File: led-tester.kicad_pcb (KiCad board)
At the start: 2 copper layers, 79.7 x 19.1 mm, 23 parts, among them M1 Arduino_Mini, U1 PCF8591

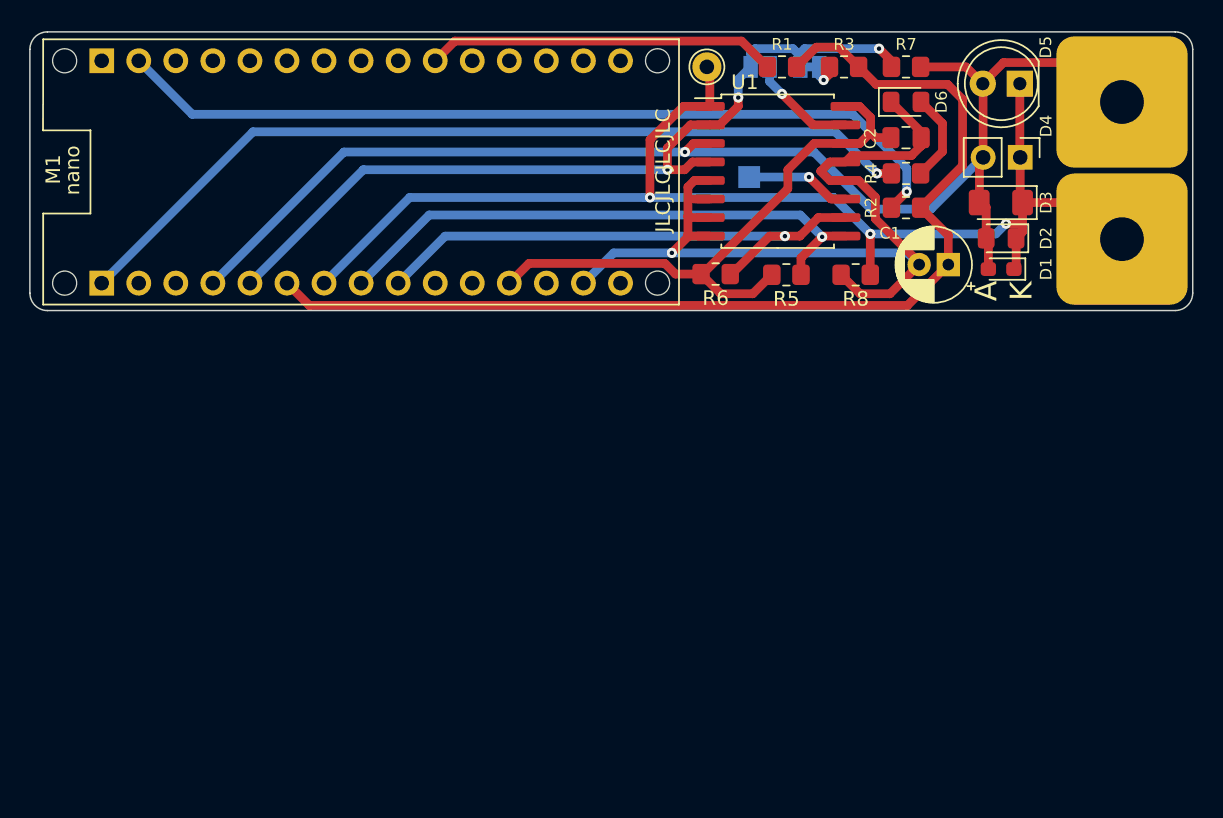
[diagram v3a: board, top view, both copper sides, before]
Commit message: Complete redesign to add op-amp buffer, 2-stage LP filter and fit in 5x5cm.
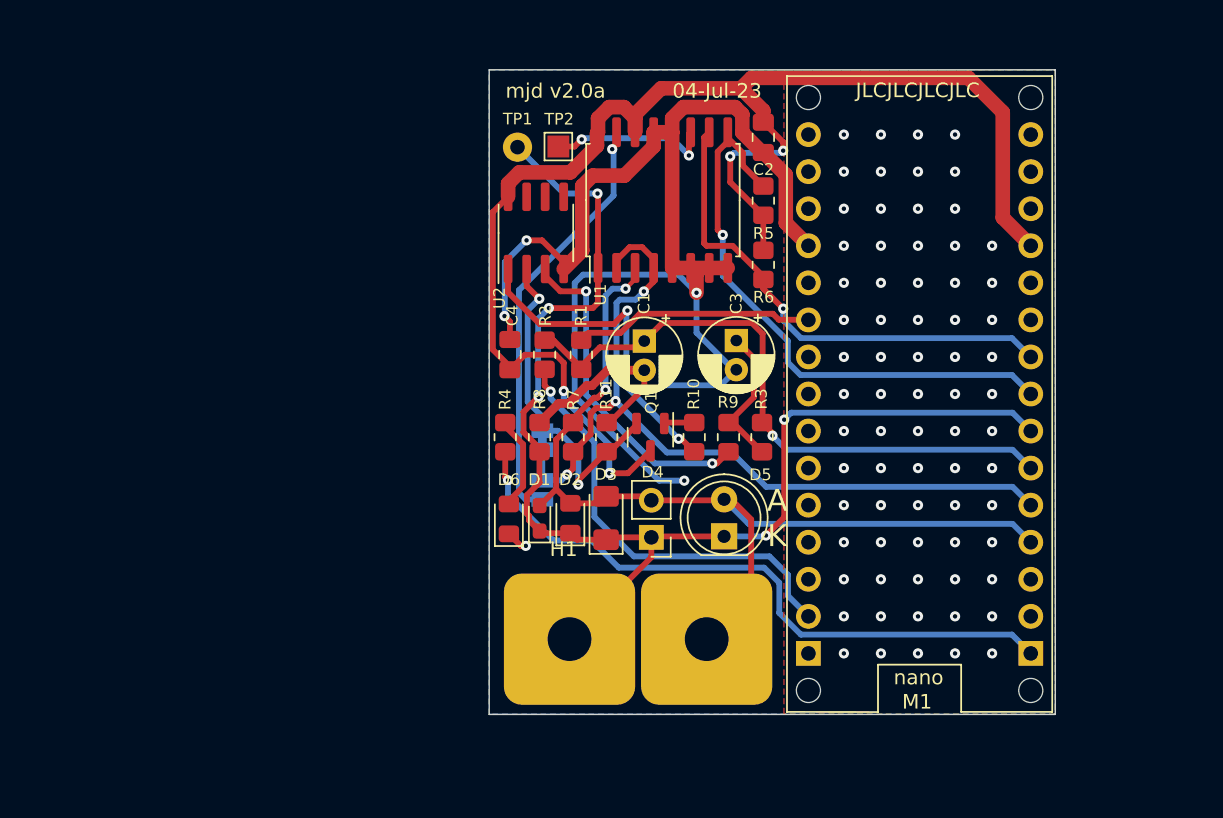
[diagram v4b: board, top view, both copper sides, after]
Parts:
- added C3: 10u, Capacitor_THT:CP_Radial_D5.0mm_P2.00mm, F.Cu at (150.4, 102.7)
- added C4: 100n, Capacitor_SMD:C_0805_2012Metric_Pad1.18x1.45mm_HandSolder, F.Cu at (134.9, 103.6)
- added H1: MountingHole, aalib:AlignmentSlot, F.Cu at (138.6, 117.5)
- added Q1: MMBT3904, Package_TO_SOT_SMD:SOT-23, F.Cu at (144.5, 109.3)
- added R10: 470R, Resistor_SMD:R_0805_2012Metric_Pad1.20x1.40mm_HandSolder, F.Cu at (147.5, 109.3)
- added R11: 1k, Resistor_SMD:R_0805_2012Metric_Pad1.20x1.40mm_HandSolder, F.Cu at (141.5, 109.3)
- added R9: 2k7, Resistor_SMD:R_0805_2012Metric_Pad1.20x1.40mm_HandSolder, F.Cu at (149.9, 109.3)
- added U2: LMV358, Package_SO:SOIC-8_3.9x4.9mm_P1.27mm, F.Cu at (136.7, 95.3)
- C1: value 100u -> 10u
- R1, R2, R3: value 100R -> 470R
- R7: value 4R7 -> 100R
- TP1: moved to B.Cu
- TP2: moved to F.Cu
- moved JP1 46.2 mm to (143.7, 123.1), turned to 0 degrees
- moved M1 41.2 mm to (163.0, 106.3), turned to 180 degrees
- moved D6 39.5 mm to (134.8, 114.9), turned to 90 degrees
- moved D5 37.1 mm to (149.6, 116.1), turned to 90 degrees
- moved D4 36.3 mm to (144.6, 116.1), turned to 180 degrees
- moved D1 35.9 mm to (136.9, 114.8), turned to 90 degrees
- moved D2 35.2 mm to (139.0, 114.8), turned to 90 degrees
- moved D3 34.6 mm to (141.5, 114.8), turned to 90 degrees
- moved R7 34.1 mm to (139.2, 109.3), turned to -90 degrees
- moved R4 32.9 mm to (134.6, 109.3), turned to -90 degrees
- moved JP3 32.6 mm to (137.1, 112.9), turned to 90 degrees
- moved JP2 31.5 mm to (137.1, 109.5), turned to -90 degrees
- moved R2 26.7 mm to (137.3, 103.6), turned to 90 degrees
- moved R3 26.0 mm to (152.2, 109.3), turned to 90 degrees
- moved R8 24.4 mm to (136.9, 109.3), turned to 90 degrees
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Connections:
- R3 pad 1: Net-(JP2-A) -> Net-(C3-Pad1)
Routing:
- net +5V: track 41.0 -> 98.6 mm, vias 0 -> 4
- net GND: track 63.6 -> 111.5 mm, vias 1 -> 77
- net /A2: track 73.8 -> 43.5 mm, vias 0 -> 1
- net /*D11/MOSI: track 58.8 -> 29.9 mm
- net /A0: track 90.6 -> 66.1 mm, vias 1 -> 2
- net Net-(U2A-+): track 0.00 -> 22.9 mm, vias 0 -> 2
- net Net-(R10-Pad2): track 0.00 -> 22.8 mm, vias 0 -> 2
- net Net-(JP3-A): track 7.43 -> 29.3 mm
- net Net-(JP2-A): track 2.09 -> 23.5 mm, vias 1 -> 2
- net /D13/SCK: track 59.6 -> 44.6 mm
- net Net-(C3-Pad1): track 0.00 -> 9.97 mm
- net /*D3: track 24.1 -> 16.5 mm
- net Net-(U1-OSC): track 7.22 -> 11.3 mm, vias 1 -> 2
- net /A5/SCL: track 37.3 -> 34.3 mm
- net Net-(Q1-B): track 0.00 -> 2.08 mm
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- added copper zone on B.Cu, net GND
- added copper zone on F.Cu, net GND
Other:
- board size 79.7 x 19.1 mm -> 38.8 x 44.2 mm
- board text added: "04-Jul-23"
- board text added: "mjd v2.0a"
- board text removed: "11-May-23"
- board text removed: "mjd v1.0f"

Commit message: Added a common-anode RGB LED.
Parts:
- added D7: LED_RAGB, aalib:LED_D8.0mm-4_RGB, F.Cu at (164.8, 126.8)
- added R12: R, Resistor_SMD:R_0603_1608Metric, F.Cu at (157.5, 117.1)
- added R13: R, Resistor_SMD:R_0603_1608Metric, F.Cu at (157.5, 120.4)
- added R14: R, Resistor_SMD:R_0603_1608Metric, F.Cu at (157.5, 123.7)
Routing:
- net +5V: track 98.6 -> 140.1 mm
- net Net-(D7-RK): track 0.00 -> 13.6 mm
- net Net-(D7-GK): track 0.00 -> 8.42 mm
- net /*D10/SS: track 0.00 -> 4.72 mm
- net Net-(D7-BK): track 0.00 -> 4.37 mm
- net /*D9: track 0.00 -> 4.01 mm
- net /D8: track 0.00 -> 3.22 mm
- net GND: vias 77 -> 73
